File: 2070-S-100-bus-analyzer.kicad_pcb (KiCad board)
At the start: 4 copper layers, 254 x 137.8 mm, 91 parts, among them J1 S-100 Edge Connector, J10 Conn_02x13_Odd_Even, J11 Conn_02x13_Odd_Even, J12 USB4105-GF-A, J13 Conn_01x01, J14 Conn_01x01, J15 Conn_01x02, J16 Conn_01x02, J17 Conn_01x02, J18 Conn_01x02, J19 Conn_01x02, J2 Conn_02x13_Odd_Even, J3 Conn_02x13_Odd_Even, J4 Conn_02x13_Odd_Even, J5 Conn_02x13_Odd_Even, J6 Conn_02x13_Odd_Even, J7 Conn_02x13_Odd_Even, J8 Conn_02x13_Odd_Even, J9 Conn_02x13_Odd_Even, SW1 SW_MEC_5E, U1 74LVCH245APW,118, U10 74LVCH245APW,118, U11 74LVCH245APW,118, U12 74LVCH245APW,118, U13 74LVCH245APW,118, U14 74LVCH245APW,118, U15 74LVCH245APW,118, U16 AP63300, U17 LMS78_05-2.0R, U2 74LVCH245APW,118, U3 74LVCH245APW,118, U4 74LVCH245APW,118, U5 74LVCH245APW,118, U6 74LVCH245APW,118, U7 74LVCH245APW,118, U8 74LVCH245APW,118, U9 74LVCH245APW,118

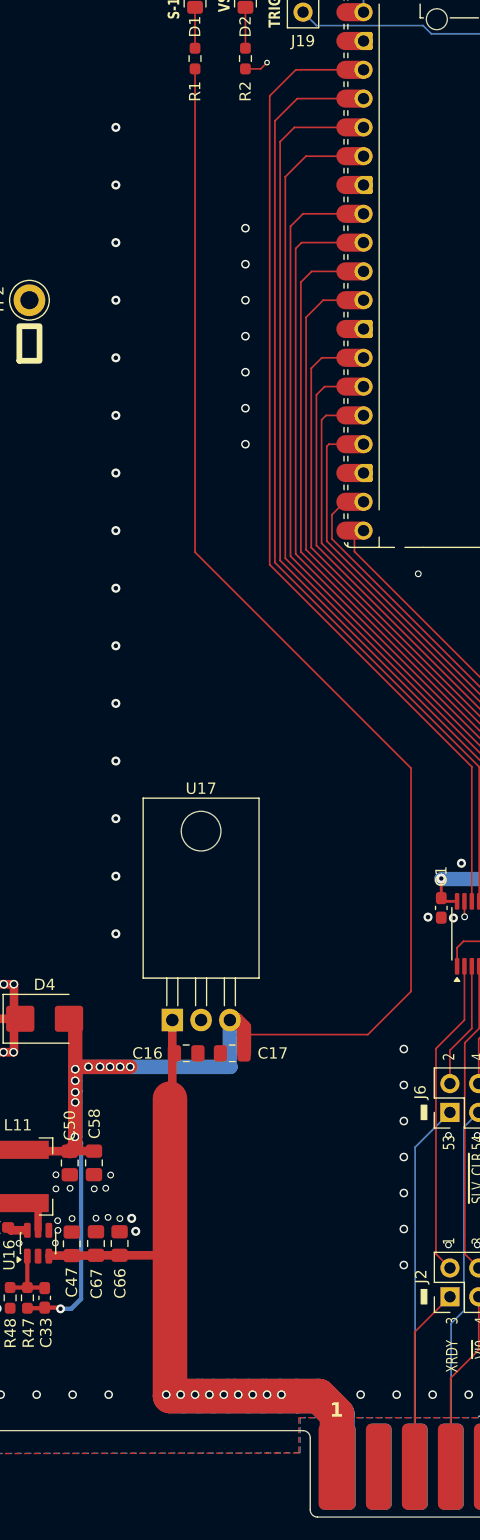
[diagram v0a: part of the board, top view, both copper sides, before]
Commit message: Remove linear regulator option
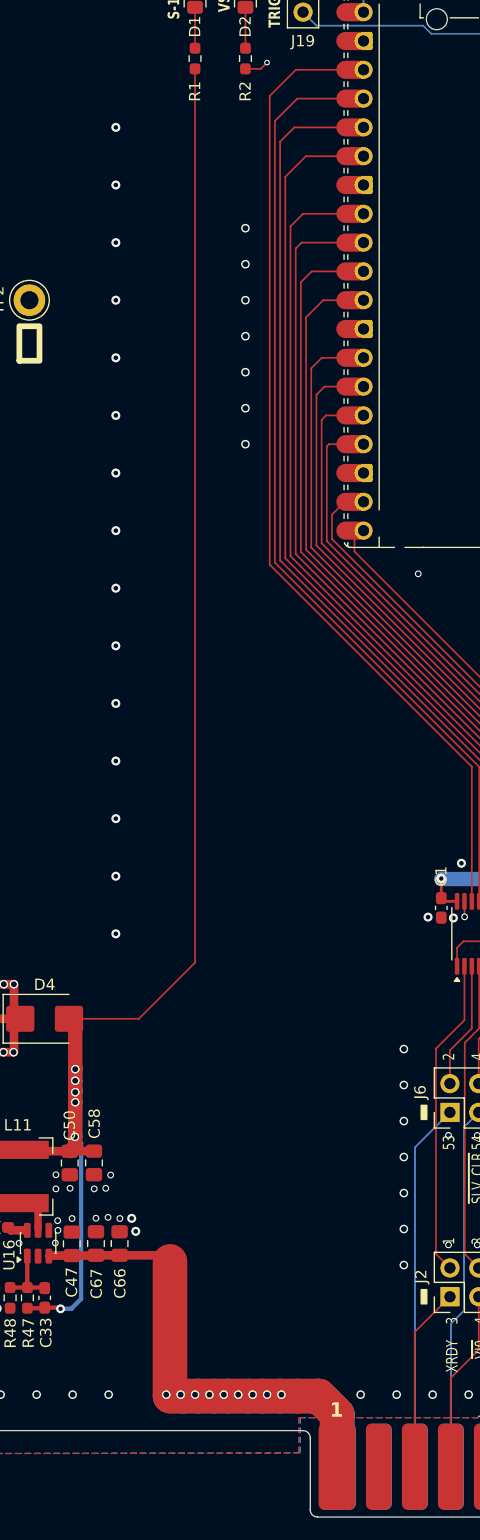
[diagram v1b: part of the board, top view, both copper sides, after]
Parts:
- removed C16: 22uF 35V, Capacitor_SMD:C_0805_2012Metric_Pad1.18x1.45mm_HandSolder
- removed C17: 22uF, Capacitor_SMD:C_0805_2012Metric_Pad1.18x1.45mm_HandSolder
- removed U17: LMS78_05-2.0R, Package_TO_SOT_THT:TO-220-3_Horizontal_TabDown
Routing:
- net +S100_5V: track 176.7 -> 136.6 mm, vias 11 -> 6
- net +S100_8V: track 98.2 -> 62.5 mm
